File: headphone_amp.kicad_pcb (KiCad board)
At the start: 2 copper layers, 25 parts, among them J1 USB4085-GF-A, J2 JST PH2, J3 JST GH2, J4 JST SH3, J5 Header_2x1, U1 BQ24074RGTR, U2 OPA1678

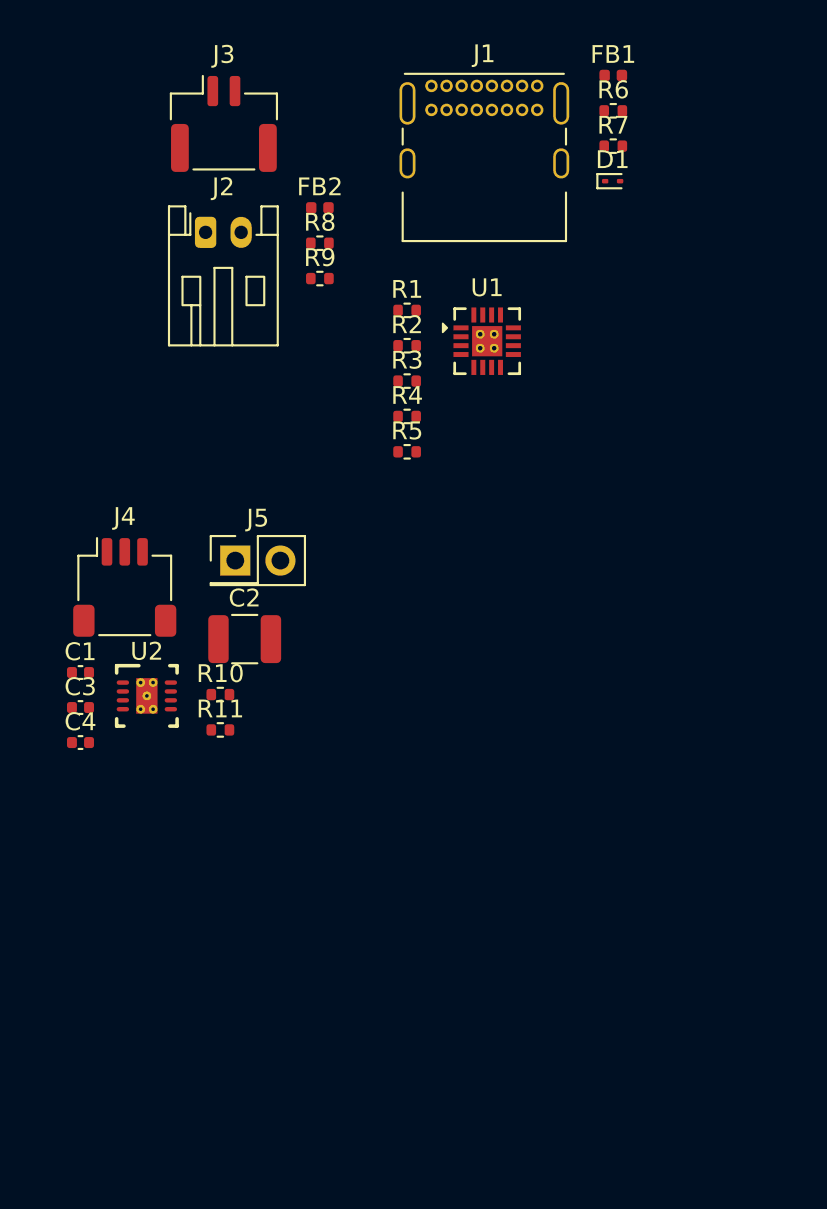
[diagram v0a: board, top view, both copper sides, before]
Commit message: Finished second stage, added diode clipping options, and started current buffer.
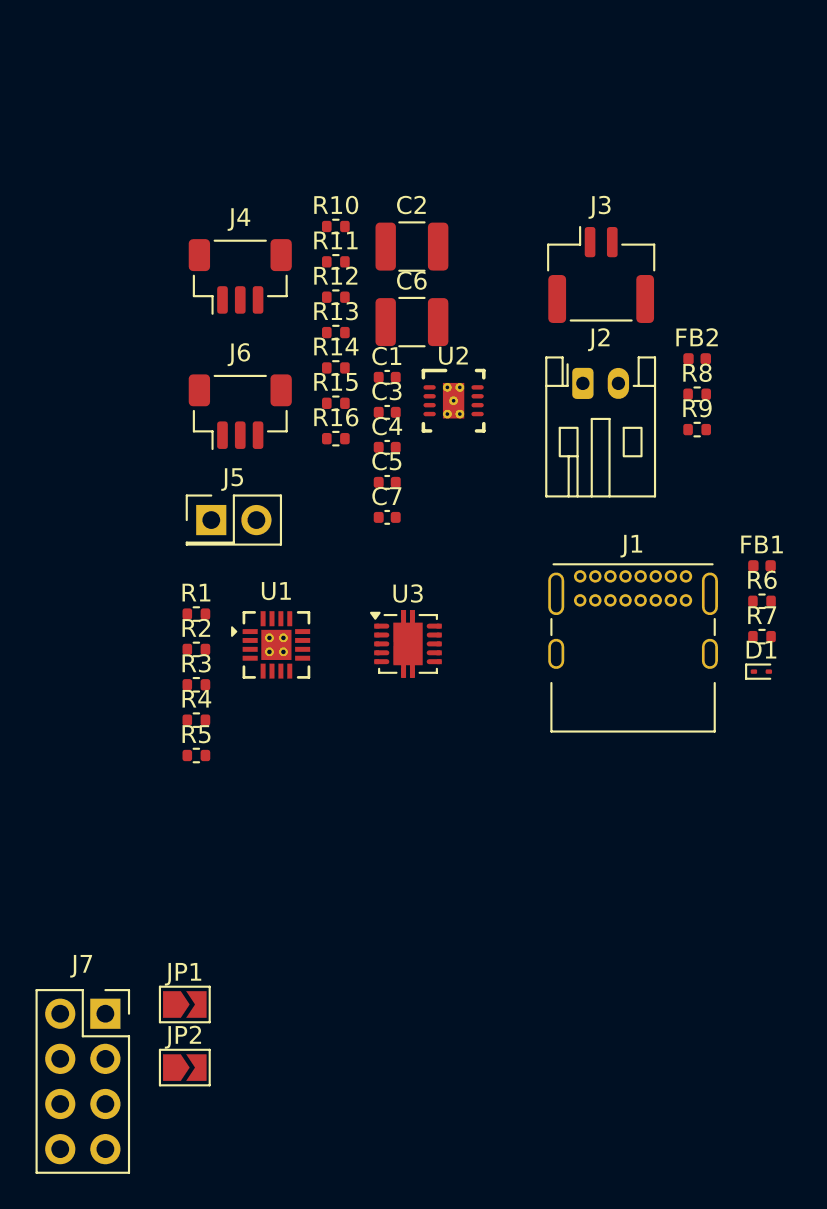
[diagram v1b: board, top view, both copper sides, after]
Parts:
- added C5: 47nF, Capacitor_SMD:C_0402_1005Metric, F.Cu at (104.7, 86.4)
- added C6: 0.1uF, Capacitor_SMD:C_1210_3225Metric, F.Cu at (106.1, 77.4)
- added C7: 51pF, Capacitor_SMD:C_0402_1005Metric, F.Cu at (104.7, 88.4)
- added J6: JST SH3, Connector_JST:JST_SH_BM03B-SRSS-TB_1x03-1MP_P1.00mm_Vertical, F.Cu at (96.4, 82.4)
- added J7: 415-47-208-41-004000, Connector_PinSocket_2.54mm:PinSocket_2x04_P2.54mm_Vertical, F.Cu at (88.8, 116.3)
- added JP1: SolderJumper_2_Open, Jumper:SolderJumper-2_P1.3mm_Open_TrianglePad1.0x1.5mm, F.Cu at (93.3, 115.8)
- added JP2: SolderJumper_2_Open, Jumper:SolderJumper-2_P1.3mm_Open_TrianglePad1.0x1.5mm, F.Cu at (93.3, 119.3)
- added R12: 4.7K, Resistor_SMD:R_0402_1005Metric, F.Cu at (101.8, 76.0)
- added R13: 1M, Resistor_SMD:R_0402_1005Metric, F.Cu at (101.8, 78.0)
- added R14: 100K, Resistor_SMD:R_0402_1005Metric, F.Cu at (101.8, 80.0)
- added R15: 33K, Resistor_SMD:R_0402_1005Metric, F.Cu at (101.8, 81.9)
- added R16: 33K, Resistor_SMD:R_0402_1005Metric, F.Cu at (101.8, 83.9)
- added U3: OPA1622, Package_SON:Texas_S-PVSON-N10, F.Cu at (105.9, 95.5)
- J4: footprint Connector_JST:JST_SH_SM03B-SRSS-TB_1x03-1MP_P1.00mm_Horizontal -> Connector_JST:JST_SH_BM03B-SRSS-TB_1x03-1MP_P1.00mm_Vertical
- moved D1 28.8 mm to (125.8, 97.0)
- moved J1 28.8 mm to (115.6, 91.7)
- moved R7 28.8 mm to (125.8, 95.1)
- moved FB1 28.8 mm to (125.8, 91.1)
- moved R6 28.8 mm to (125.8, 93.1)
- moved R11 27.1 mm to (101.8, 74.0)
- moved R10 27.1 mm to (101.8, 72.0)
- moved C2 24.0 mm to (106.1, 73.1)
- moved U2 24.0 mm to (108.4, 81.8)
- moved C1 24.0 mm to (104.7, 80.5)
- moved C3 24.0 mm to (104.7, 82.5)
- moved C4 24.0 mm to (104.7, 84.4)
- moved FB2 22.9 mm to (122.1, 79.4)
- moved J2 22.9 mm to (115.7, 80.8)
- moved J3 22.9 mm to (116.7, 74.7)
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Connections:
- U2 pad 5: unconnected-(U2B-+-Pad5) -> Net-(U2B-+)
- U2 pad 6: unconnected-(U2B---Pad6) -> /Audio Input/SECOND_STAGE_IN
- U2 pad 7: unconnected-(U2-Pad7) -> /Audio Input/SECOND_STAGE_OUT

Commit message: Added notes and started work on boost converter.
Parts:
- added D2: D, Diode_SMD:D_SOD-123, F.Cu at (119.9, 114.7)
- added D3: D, Diode_SMD:D_SOD-123, F.Cu at (119.9, 118.0)
- added L1: 3.3uH, Inductor_SMD:L_1008_2520Metric, F.Cu at (112.0, 119.8)
- added U5: TPS61379QWRTERQ1, integrated_circuits:VREG_TPS61379QWRTERQ1, F.Cu at (112.5, 115.5)

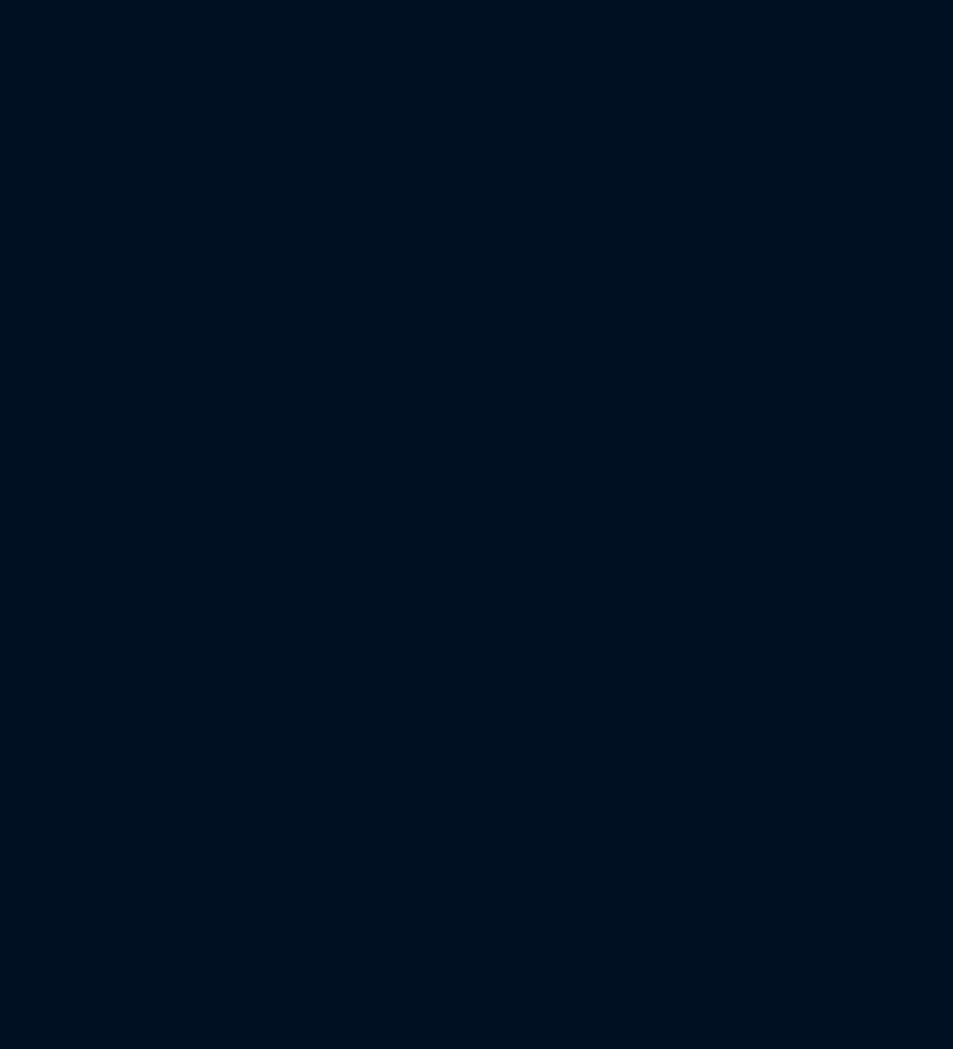
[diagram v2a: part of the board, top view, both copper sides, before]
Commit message: First rough draft of schematics complete -- missing a lot of PLM/Inventree work. Ran through several Claude reviews.
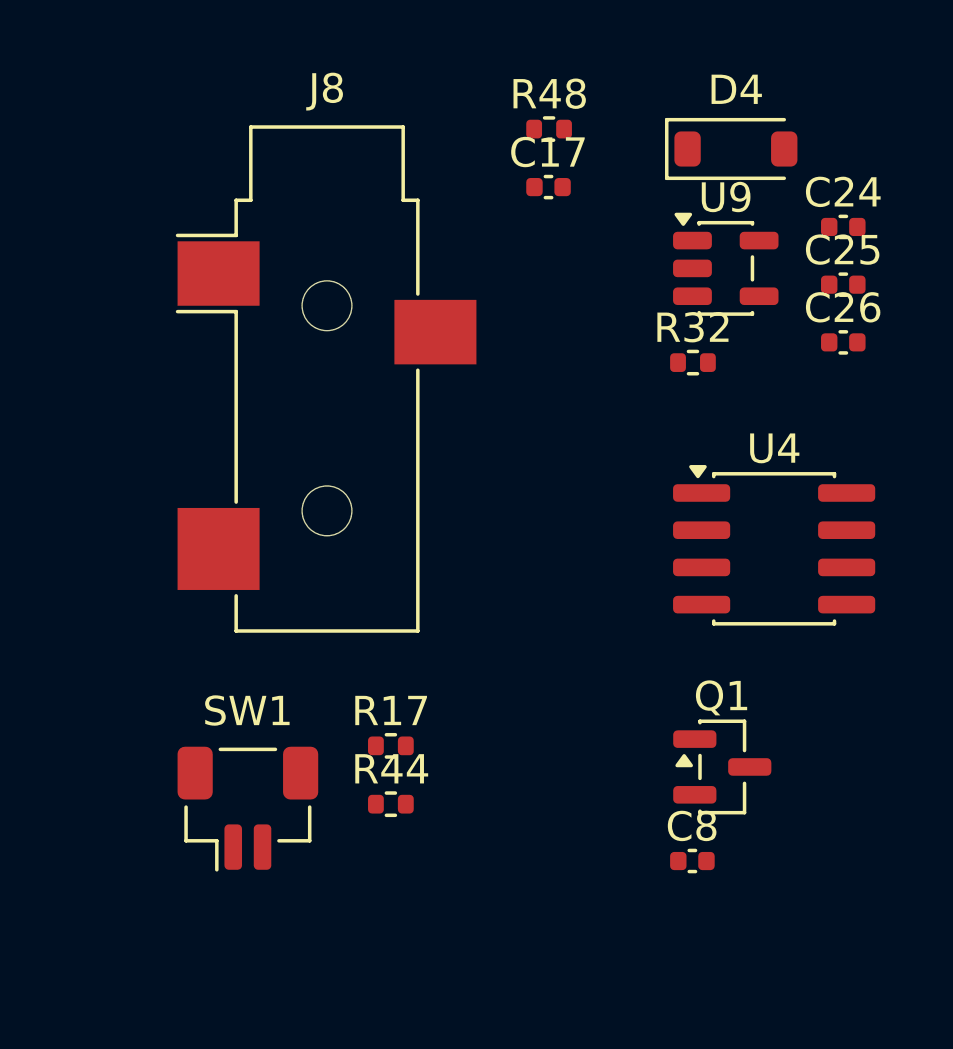
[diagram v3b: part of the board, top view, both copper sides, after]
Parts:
- added C17: 0.1uF, Capacitor_SMD:C_0402_1005Metric, F.Cu at (157.7, 72.0)
- added C24: 0.1uF, Capacitor_SMD:C_0402_1005Metric, F.Cu at (167.7, 73.3)
- added C25: 0.1uF, Capacitor_SMD:C_0402_1005Metric, F.Cu at (167.7, 75.3)
- added C26: 0.1uF, Capacitor_SMD:C_0402_1005Metric, F.Cu at (167.7, 77.3)
- added C8: 0.1uF, Capacitor_SMD:C_0402_1005Metric, F.Cu at (162.6, 95.0)
- added D4: 1N4148W-7-F, Diode_SMD:D_SOD-123, F.Cu at (164.1, 70.7)
- added J8: AudioPlug3, Connector_Audio:Jack_3.5mm_CUI_SJ-3523-SMT_Horizontal, F.Cu at (150.1, 78.5)
- added Q1: BSS138, Package_TO_SOT_SMD:SOT-23, F.Cu at (163.6, 91.8)
- added R17: 3.16K, Resistor_SMD:R_0402_1005Metric, F.Cu at (152.3, 91.0)
- added R32: 100K, Resistor_SMD:R_0402_1005Metric, F.Cu at (162.6, 78.0)
- added R44: 10K, Resistor_SMD:R_0402_1005Metric, F.Cu at (152.3, 93.0)
- added R48: 100K, Resistor_SMD:R_0402_1005Metric, F.Cu at (157.7, 70.0)
- added SW1: SW_SPST, Connector_JST:JST_SH_BM02B-SRSS-TB_1x02-1MP_P1.00mm_Vertical, F.Cu at (147.4, 93.2)
- added U4: TLE2426xD, Package_SO:SOIC-8_3.9x4.9mm_P1.27mm, F.Cu at (165.4, 84.3)
- added U9: TLV7A0325PDBVR, Package_TO_SOT_SMD:SOT-23-5, F.Cu at (163.7, 74.8)
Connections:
- net /Audio Input/OUT renamed /AUDIO_BUFFER_IN
- net /Audio Input/SECOND_STAGE_OUT renamed /AUDIO_IN
- net Net-(L1-Pad1) renamed /Boost/SW
- C1 pad 1: /Audio Input/V_{+} -> /V+
- C5 pad 2: /Audio Input/V_{MID} -> /V_{MID}
- D2 pad 1: /Audio Input/V_{MID} -> /V_{MID}
- D3 pad 2: /Audio Input/V_{MID} -> /V_{MID}
- FB1 pad 2: /Power Input/VBUS -> /V_{BUS}
- FB2 pad 2: /Battery/V_{BAT} -> /V_{BAT}
- J6 pad 1: /Audio Input/V_{MID} -> /V_{MID}
- L1 pad 2: unconnected-(L1-Pad2) -> /Boost/Vin
- R13 pad 1: /Audio Input/V_{MID} -> /V_{MID}
- R16 pad 1: /Audio Input/V_{MID} -> /V_{MID}
- R8 pad 2: /Battery/BAT_THERMISTOR+ -> /TS+
- R9 pad 2: /Battery/BAT_THERMISTOR- -> GND
- U1 pad 1: unconnected-(U1-TS-Pad1) -> /TS+
- U1 pad 12: unconnected-(U1-ILIM-Pad12) -> /Battery Charger/ILIM
- U1 pad 13: unconnected-(U1-IN-Pad13) -> /V_{BUS}
- U1 pad 14: unconnected-(U1-TMR-Pad14) -> /Battery Charger/TMR
- U1 pad 15: unconnected-(U1-ITERM-Pad15) -> /Battery Charger/ITERM
- U1 pad 16: unconnected-(U1-ISET-Pad16) -> /Battery Charger/ISET
- U1 pad 2: unconnected-(U1-BAT_2-Pad2) -> /V_{BAT}
- U1 pad 3: unconnected-(U1-BAT_3-Pad3) -> /V_{BAT}
- U1 pad 7: unconnected-(U1-~{PGOOD}-Pad7) -> Net-(D6-K)
- U1 pad 9: unconnected-(U1-~{CHG}-Pad9) -> Net-(D5-K)
- U2 pad 8: /Audio Input/V_{+} -> /V+
- U3 pad 1: unconnected-(U3A-+-Pad1) -> /Current Buffer/LEFT_IN
- U3 pad 10: unconnected-(U3A---Pad10) -> /Current Buffer/FB_L
- U3 pad 11: Net-(U3C-V--Pad11) -> GND
- U3 pad 2: unconnected-(U3C-V+-Pad2) -> /V+
- U3 pad 3: unconnected-(U3C-GND-Pad3) -> /V_{MID}
- U3 pad 4: Net-(U3C-V--Pad11) -> GND
- U3 pad 5: unconnected-(U3B-+-Pad5) -> /Current Buffer/RIGHT_IN
- U3 pad 6: unconnected-(U3B---Pad6) -> /Current Buffer/FB_R
- U3 pad 7: unconnected-(U3-Pad7) -> /Current Buffer/RIGHT_OUT
- U3 pad 8: unconnected-(U3A-EN-Pad8) -> /Current Buffer/EN
- U3 pad 9: unconnected-(U3-Pad9) -> /Current Buffer/LEFT_OUT
- U5 pad 1: unconnected-(U5-VIN-Pad1) -> /Boost/Vin
- U5 pad 10: unconnected-(U5-OUT-Pad10) -> /Boost/OUT
- U5 pad 11: unconnected-(U5-PG-Pad11) -> /Boost/PG
- U5 pad 13: unconnected-(U5-FB-Pad13) -> /Boost/FB
- U5 pad 14: unconnected-(U5-COMP-Pad14) -> /Boost/COMP
- U5 pad 15: unconnected-(U5-EN-Pad15) -> /Boost/EN
- U5 pad 16: unconnected-(U5-FREQ-Pad16) -> /Boost/FREQ
- U5 pad 17: unconnected-(U5-EXP-Pad17) -> GND
- U5 pad 2: unconnected-(U5-BST-Pad2) -> /Boost/BST
- U5 pad 5: unconnected-(U5-MODE/SYNC-Pad5) -> /Boost/MODE
- U5 pad 6: unconnected-(U5-VCC-Pad6) -> /Boost/VCC
- U5 pad 7: unconnected-(U5-GND-Pad7) -> GND
- U5 pad 8: unconnected-(U5-GND-Pad8) -> GND
- U5 pad 9: unconnected-(U5-VO-Pad9) -> /V+

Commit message: Started Inventree work.
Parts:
- added C18: 220uF, cap_polymer:WCAP-PSLP_6.3X5.8_DXL_, F.Cu at (149.3, 112.7)
- added C19: 220uF, cap_polymer:WCAP-PSLP_6.3X5.8_DXL_, F.Cu at (149.3, 121.0)
- added C34: 0.1uF, Capacitor_SMD:C_0402_1005Metric, F.Cu at (156.0, 109.5)
- added C35: 0.1uF, Capacitor_SMD:C_0402_1005Metric, F.Cu at (156.0, 111.5)
- added D5: IN-S42ATA, LED_SMD:LED_0402_1005Metric, F.Cu at (161.2, 109.5)
- added D6: IN-S42ATA, LED_SMD:LED_0402_1005Metric, F.Cu at (161.2, 111.5)
- added FB3: MDF2016BSS600CTD25, Inductor_SMD:L_Wuerth_PMFI-201610, F.Cu at (146.0, 128.8)
- added R33: 33R, Resistor_SMD:R_0402_1005Metric, F.Cu at (160.9, 119.5)
- added R34: 33R, Resistor_SMD:R_0402_1005Metric, F.Cu at (160.9, 121.5)
- added R35: 33R, Resistor_SMD:R_0402_1005Metric, F.Cu at (160.9, 123.4)
- added R38: 33R, Resistor_SMD:R_0402_1005Metric, F.Cu at (160.9, 125.4)
- added R47: 33R, Resistor_SMD:R_0402_1005Metric, F.Cu at (160.9, 127.4)
- added R53: 100K, Resistor_SMD:R_0402_1005Metric, F.Cu at (160.9, 115.5)
- J8: value AudioPlug3 -> AudioJack3
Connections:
- net /AUDIO_IN renamed /WD_AUDIO_IN
- net /Current Buffer/LEFT_OUT renamed /Current Buffer/S_LEFT_OUT
- net /Current Buffer/RIGHT_OUT renamed /Current Buffer/S_RIGHT_OUT
- J8 pad R: Net-(C19-Pad2) -> /Current Buffer/HEADPHONES_RIGHT
- J8 pad T: Net-(C18-Pad2) -> /Current Buffer/HEADPHONES_LEFT
- Q1 pad 1: Net-(Q1-G) -> /SHUTDOWN
- U1 pad 7: Net-(D6-K) -> /Battery Charger/~{PGOOD}
- U1 pad 9: Net-(D5-K) -> /Battery Charger/~{CHG}

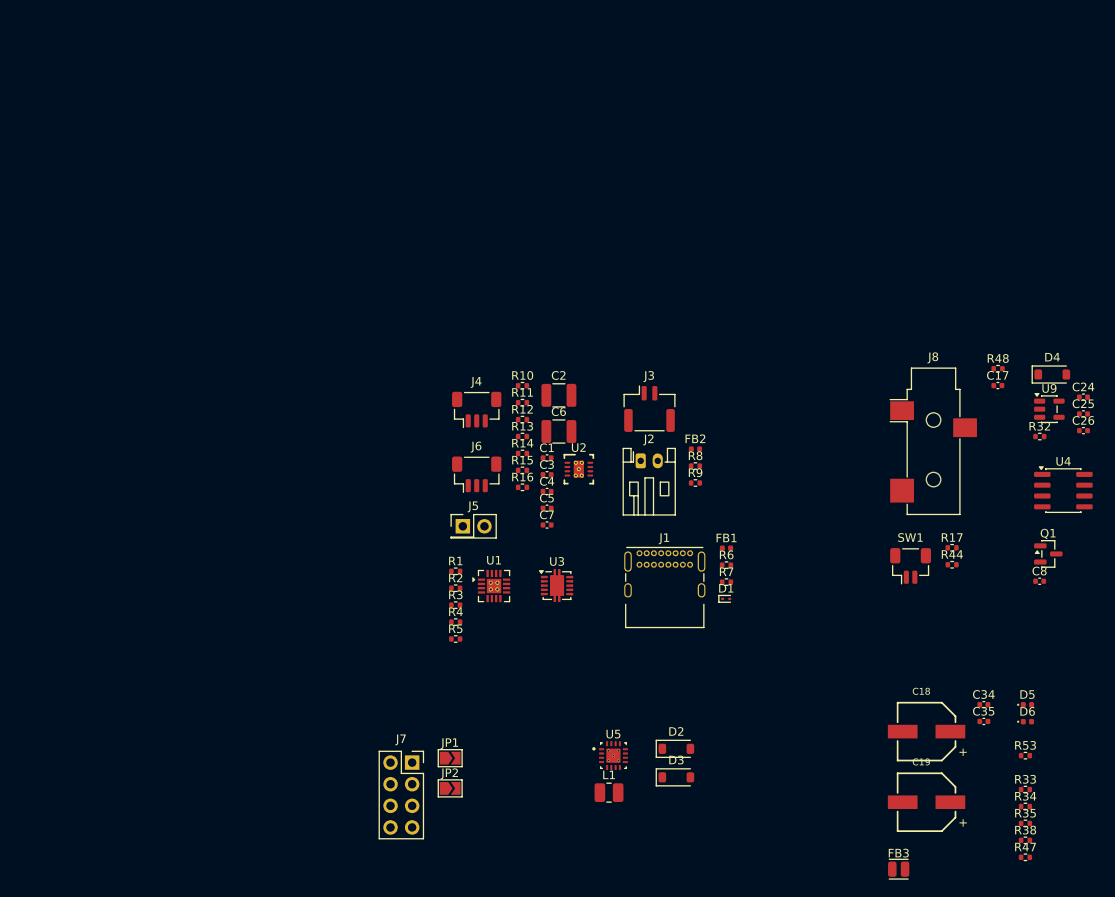
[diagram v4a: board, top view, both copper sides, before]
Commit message: Updated theory doc, started layout, fixed a footprint.
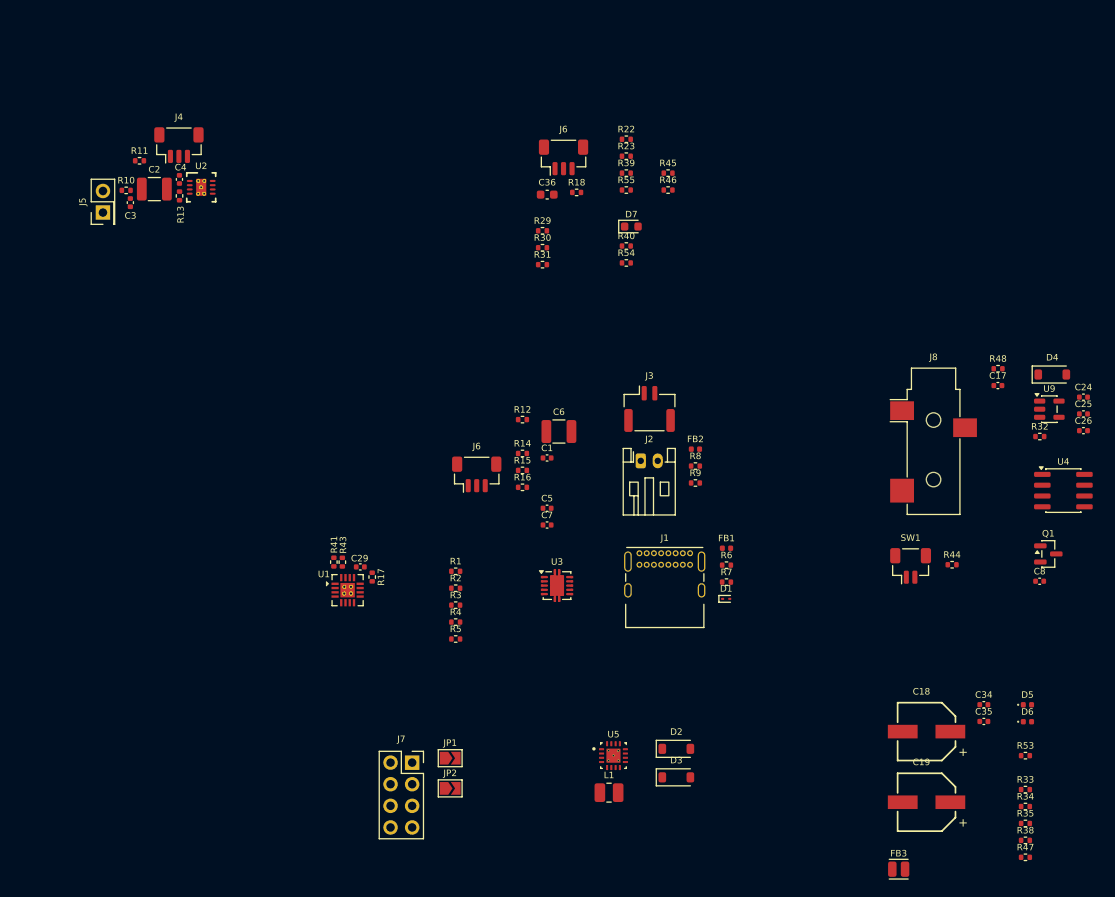
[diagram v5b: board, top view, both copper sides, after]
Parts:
- added C29: 1uF, Capacitor_SMD:C_0402_1005Metric, F.Cu at (82.7, 93.3)
- added C36: 3.9nF, Capacitor_SMD:C_0603_1608Metric, F.Cu at (104.7, 49.5)
- added D7: CD0603-B0340R, Diode_SMD:D_0603_1608Metric, F.Cu at (114.6, 53.3)
- added J6: JST SH3, Connector_JST:JST_SH_BM03B-SRSS-TB_1x03-1MP_P1.00mm_Vertical, F.Cu at (106.6, 45.1)
- added R18: 10K, Resistor_SMD:R_0402_1005Metric, F.Cu at (108.2, 49.3)
- added R22: 80.6K, Resistor_SMD:R_0402_1005Metric, F.Cu at (114.0, 43.0)
- added R23: 825K, Resistor_SMD:R_0402_1005Metric, F.Cu at (114.0, 45.0)
- added R29: 470K, Resistor_SMD:R_0402_1005Metric, F.Cu at (104.2, 53.8)
- added R30: 470K, Resistor_SMD:R_0402_1005Metric, F.Cu at (104.2, 55.8)
- added R31: 470K, Resistor_SMD:R_0402_1005Metric, F.Cu at (104.2, 57.8)
- added R39: 470K, Resistor_SMD:R_0402_1005Metric, F.Cu at (114.0, 47.0)
- added R40: 100K, Resistor_SMD:R_0402_1005Metric, F.Cu at (114.0, 55.6)
- added R41: 4.42K, Resistor_SMD:R_0402_1005Metric, F.Cu at (79.6, 92.7)
- added R43: 4.42K, Resistor_SMD:R_0402_1005Metric, F.Cu at (80.6, 92.7)
- added R45: 1.5K, Resistor_SMD:R_0402_1005Metric, F.Cu at (118.9, 47.0)
- added R46: 1.5K, Resistor_SMD:R_0402_1005Metric, F.Cu at (118.9, 49.0)
- added R54: 100K, Resistor_SMD:R_0402_1005Metric, F.Cu at (114.0, 57.6)
- added R55: 1M, Resistor_SMD:R_0402_1005Metric, F.Cu at (114.0, 49.0)
- C7: value 51pF -> 470pF
- J8: value AudioJack3 -> SJ-3523-SMT-TR
- moved R17 68.3 mm to (84.1, 94.5), turned to 90 degrees
- moved C3 58.5 mm to (55.7, 50.5), turned to -90 degrees
- moved C4 56.7 mm to (61.5, 47.7), turned to 90 degrees
- moved J5 56.1 mm to (52.5, 51.6), turned to 90 degrees
- moved U2 55.4 mm to (64.0, 48.7)
- moved C2 53.4 mm to (58.5, 48.9)
- moved R11 53.2 mm to (56.8, 45.5)
- moved R10 51.9 mm to (55.2, 49.0)
- moved R13 49.2 mm to (61.5, 49.7), turned to 90 degrees
- moved J4 46.8 mm to (61.4, 43.7)
- moved U1 17.2 mm to (81.2, 96.0)
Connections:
- C1 pad 1: /V+ -> /Audio Input/V_{+}F
- FB3 pad 2: /V+ -> /Audio Input/V_{+}F
- U2 pad 8: /V+ -> /Audio Input/V_{+}F
